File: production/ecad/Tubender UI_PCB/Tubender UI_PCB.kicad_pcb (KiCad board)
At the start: 2 copper layers, 7 parts, among them J1 640387-5, J2 1-640387-0

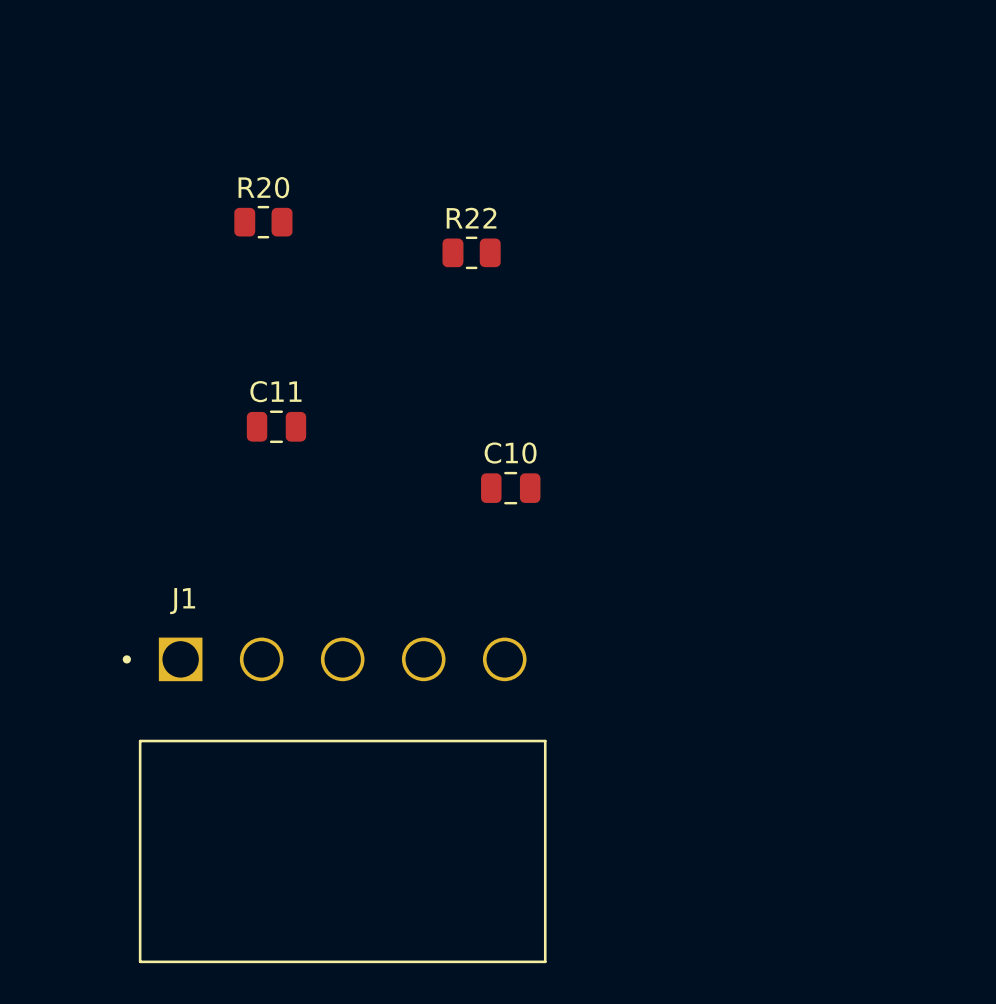
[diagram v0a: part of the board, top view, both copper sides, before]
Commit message: Some intial work for rotary encoder on  PCB
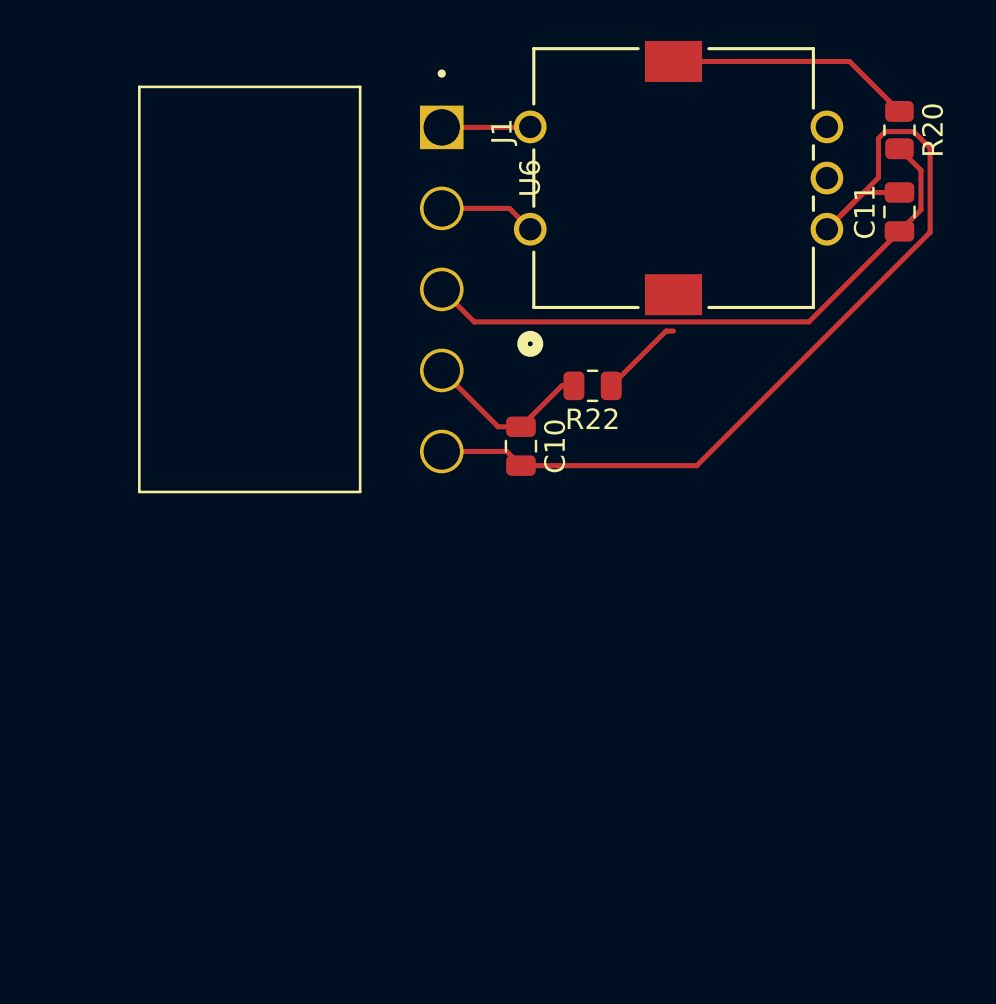
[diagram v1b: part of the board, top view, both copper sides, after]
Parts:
- added U6: PEC11R-4215K-S0024, Rotary_Encoder:SW_PEC11R-4XXXK-SXXXX_BRN, F.Cu at (217.5, 26.8)
- moved C11 32.2 mm to (235.5, 26.0), turned to 90 degrees
- moved R20 31.4 mm to (235.5, 22.0), turned to -90 degrees
- moved J1 29.0 mm to (213.1, 21.9), turned to -90 degrees
- moved R22 8.79 mm to (220.5, 34.5), turned to 180 degrees
- moved C10 2.11 mm to (217.0, 37.5), turned to -90 degrees
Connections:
- C10 pad 2: GND -> +3V3
- C11 pad 2: GND -> +3V3
- C18 pad 2: GND -> +3V3
- J1 pad 5: GND -> +3V3
- J2 pad 10: GND -> +3V3
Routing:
- net +3V3: track 0.00 -> 45.8 mm
- net DIAL_CHANNEL_B: track 0.00 -> 29.8 mm
- net Net-(U6-B): track 0.00 -> 12.1 mm
- net DIAL_CHANNEL_A: track 0.00 -> 8.43 mm
- net DIAL_BUTTON: track 0.00 -> 4.75 mm
- net +5V: track 0.00 -> 4.33 mm
- net Net-(U6-A): track 0.00 -> 4.15 mm

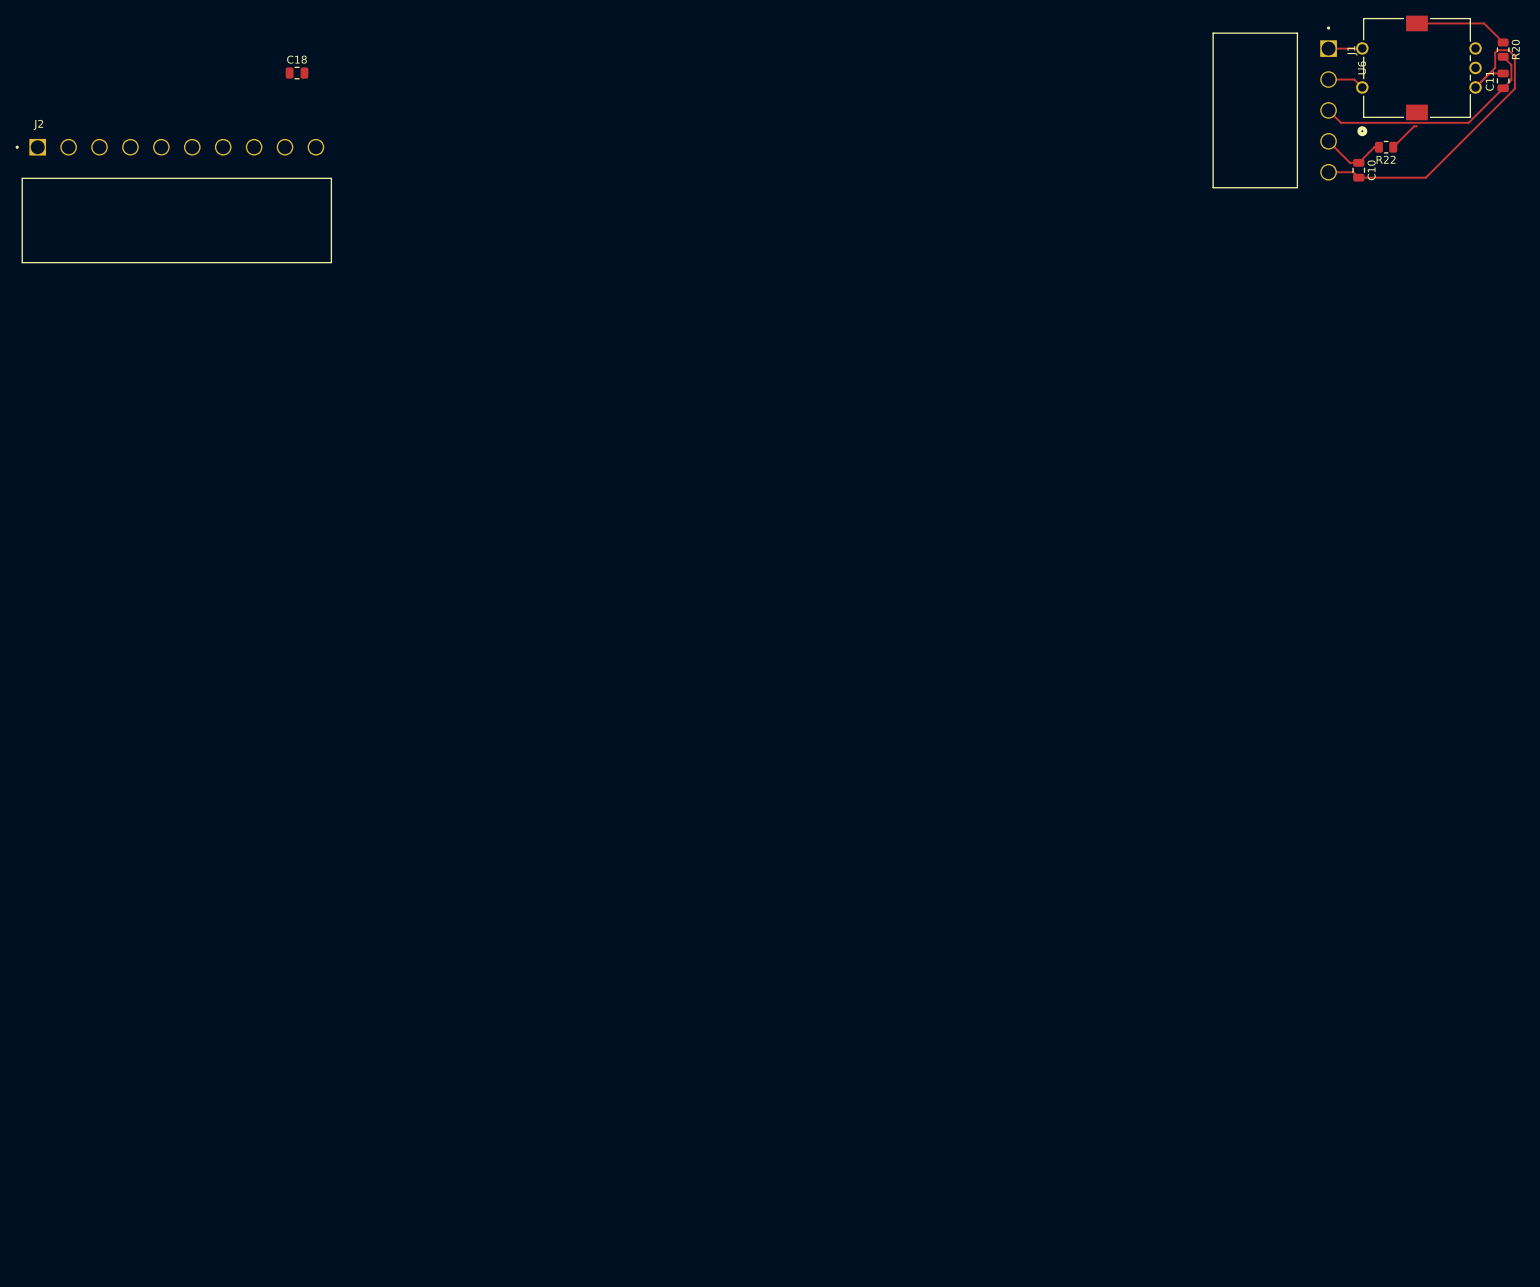
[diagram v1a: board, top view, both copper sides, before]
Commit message: Added UI footprints and first draft of layout
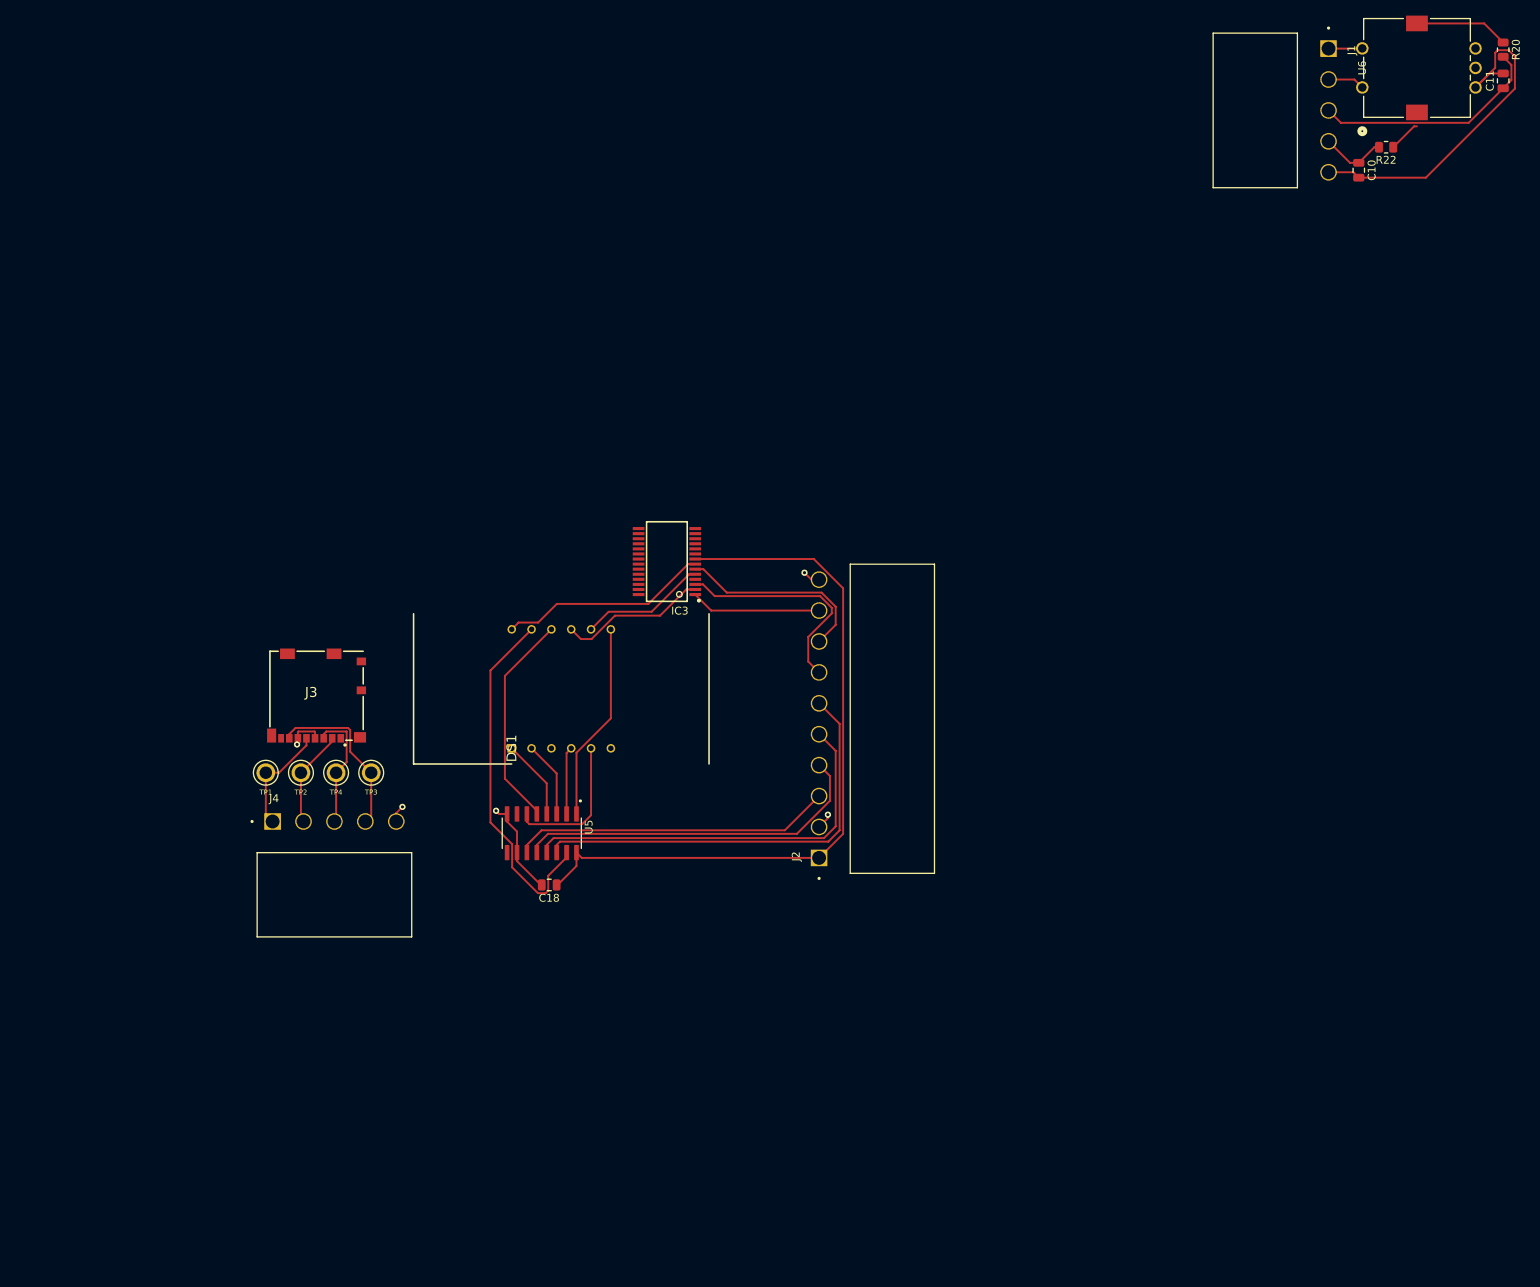
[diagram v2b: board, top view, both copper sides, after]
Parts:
- added DS1: BC56-12EWA, footprints:DIPS1524W50P254L3760H835Q12N, F.Cu at (108.5, 111.5)
- added IC3: SN74LVC1G29DCTR, footprints:SOP65P780X200-28N, F.Cu at (128.4, 87.6)
- added J3: 104031-0811, footprints:1040310811, F.Cu at (83.5, 110.5)
- added J4: 640387-5, footprints:TE_640387-5, F.Cu at (77.9, 120.9)
- added TP1: 5006, footprints:KEYSTONE_5006, F.Cu at (77.0, 114.6)
- added TP2: 5006, footprints:KEYSTONE_5006, F.Cu at (81.5, 114.6)
- added TP3: 5006, footprints:KEYSTONE_5006, F.Cu at (90.5, 114.6)
- added TP4: 5006, footprints:KEYSTONE_5006, F.Cu at (86.0, 114.6)
- added U5: 74HC595, footprints:SOIC127P600X175-16N, F.Cu at (112.3, 122.4)
- moved J2 135.3 mm to (147.9, 125.5), turned to 90 degrees
- moved C18 108.9 mm to (113.3, 129.0), turned to 180 degrees
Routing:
- net +5V: track 4.33 -> 97.3 mm
- net 7-SEG_SER: track 0.00 -> 55.4 mm
- net 7-SEG_OEb: track 0.00 -> 51.7 mm
- net 7-SEG_RCLK: track 0.00 -> 46.0 mm
- net Net-(DS1-ANODE_A): track 0.00 -> 45.8 mm
- net 7-SEG_SRCLK: track 0.00 -> 41.0 mm
- net 7-SEG_A0: track 0.00 -> 28.8 mm
- net Net-(DS1-ANODE_F): track 0.00 -> 27.8 mm
- net Net-(DS1-COMMON_CATHODE_DIG1): track 0.00 -> 27.0 mm
- net Net-(DS1-ANODE_B): track 0.00 -> 25.5 mm
- net 7-SEG_A1: track 0.00 -> 25.3 mm
- net +3V3: track 45.8 -> 69.8 mm, vias 0 -> 5
- net SD_DAT0: track 0.00 -> 21.9 mm
- net Net-(DS1-COMMON_CATHODE_DIG2): track 0.00 -> 19.0 mm
- net Net-(DS1-ANODE_G): track 0.00 -> 18.4 mm
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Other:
- copper layers 2 -> 4

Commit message: Added Display Daughter Board PCB and start UI layout
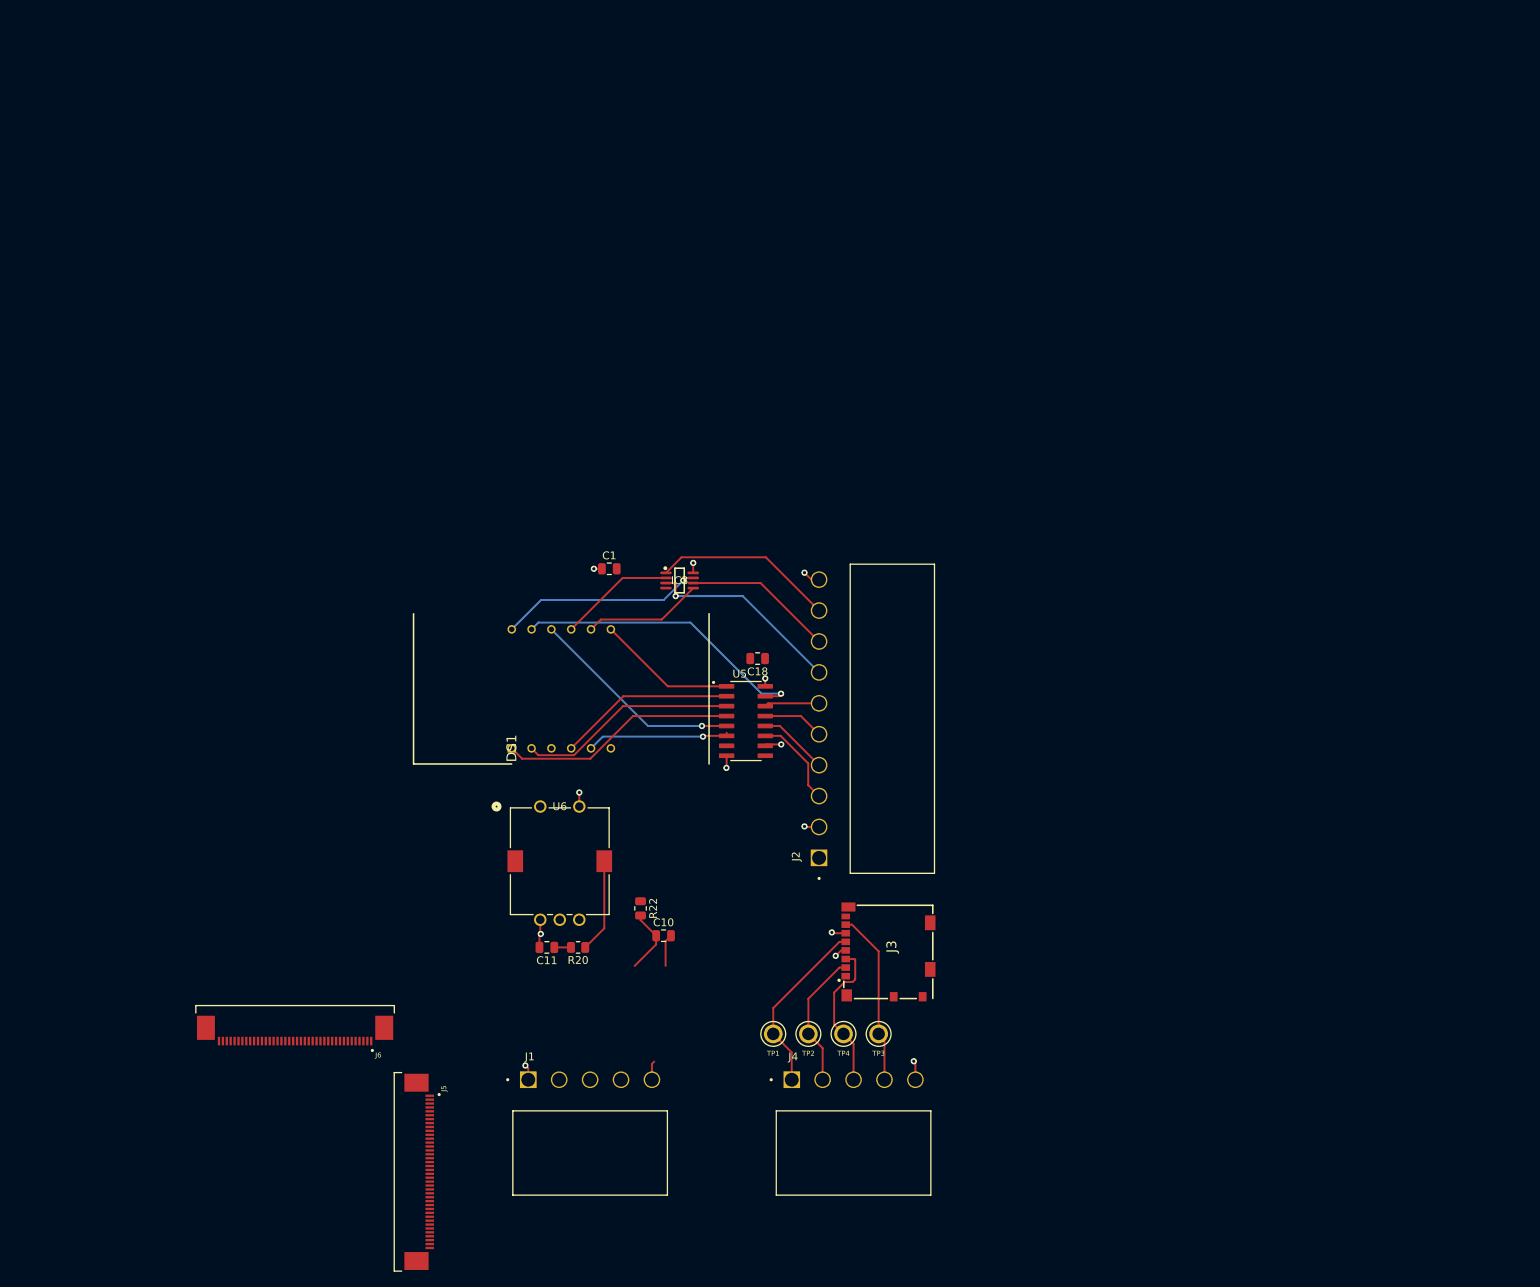
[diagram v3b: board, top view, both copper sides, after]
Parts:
- added C1: 0.1u, Capacitor_SMD:C_0805_2012Metric, F.Cu at (121.0, 88.5)
- added J5: 4-1734592-0, footprints:TE_4-1734592-0, F.Cu at (98.0, 165.8)
- added J6: 4-1734592-0, footprints:TE_4-1734592-0, F.Cu at (80.8, 149.0)
- IC3: footprint footprints:SOP65P780X200-28N -> footprints:DCT0008A_N
- moved J1 167.2 mm to (110.6, 153.9), turned to 0 degrees
- moved C11 165.3 mm to (113.0, 137.0), turned to 180 degrees
- moved R20 165.1 mm to (117.0, 137.0), turned to 180 degrees
- moved U6 139.9 mm to (112.2, 119.0), turned to 0 degrees
- moved R22 136.5 mm to (125.0, 132.0), turned to -90 degrees
- moved C10 132.5 mm to (128.0, 135.5), turned to 0 degrees
- moved J4 74.3 mm to (144.4, 153.9)
- moved TP1 73.1 mm to (142.0, 148.1)
- moved TP2 73.1 mm to (146.5, 148.1)
- moved TP3 73.1 mm to (155.5, 148.1)
- moved TP4 73.1 mm to (151.0, 148.1)
- moved J3 72.8 mm to (151.0, 137.6), turned to -90 degrees
- moved C18 39.4 mm to (140.0, 100.0)
- moved U5 29.8 mm to (138.5, 108.0), turned to 0 degrees
- moved IC3 2.92 mm to (130.0, 90.0), turned to 0 degrees
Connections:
- C10 pad 2: +3V3 -> GND
- C11 pad 2: +3V3 -> GND
- C18 pad 2: +3V3 -> GND
- IC3 pad 4: +3V3 -> GND
- J1 pad 5: +3V3 -> GND
- J2 pad 10: +3V3 -> GND
- J3 pad 6: +3V3 -> GND
- J4 pad 5: +3V3 -> GND
- U5 pad 8: +3V3 -> GND
- U6 pad 5: +3V3 -> GND
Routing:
- net +5V: track 97.3 -> 6.13 mm, vias 0 -> 4
- net +3V3: track 69.8 -> 6.06 mm, vias 5 -> 4
- net 7-SEG_SER: track 55.4 -> 7.05 mm
- net 7-SEG_OEb: track 51.7 -> 7.86 mm
- net 7-SEG_RCLK: track 46.0 -> 8.97 mm
- net 7-SEG_SRCLK: track 41.0 -> 11.7 mm
- net DIAL_CHANNEL_B: track 29.8 -> 2.14 mm
- net Net-(DS1-ANODE_E): track 10.3 -> 30.3 mm
- net GND: track 0.00 -> 18.4 mm, vias 0 -> 5
- net Net-(DS1-ANODE_D): track 9.74 -> 27.9 mm
- net Net-(DS1-ANODE_C): track 8.65 -> 22.7 mm
- net SD_CLK: track 14.2 -> 23.0 mm
- net Net-(DS1-ANODE_B): track 25.5 -> 17.8 mm
- net Net-(DS1-ANODE_A): track 45.8 -> 38.3 mm, vias 0 -> 1
- net 7-SEG_Gb: track 16.7 -> 23.3 mm
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- added copper zone on In2.Cu, net GND

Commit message: Finished First Draft Layout of UI PCB
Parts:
- removed J5, J6: 4-1734592-0, footprints:TE_4-1734592-0
- IC3: footprint footprints:DCT0008A_N -> footprints:SOP65P400X130-8N
- moved C1 39.4 mm to (144.0, 120.5), turned to 90 degrees
- moved C10 23.6 mm to (104.5, 132.5), turned to -90 degrees
- moved R22 20.9 mm to (104.5, 127.9)
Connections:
- J2 pad 1: +5V -> GND
- J2 pad 10: GND -> +5V
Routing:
- net DIAL_BUTTON: track 0.00 -> 36.0 mm
- net DIAL_CHANNEL_A: track 8.43 -> 32.6 mm
- net DIAL_CHANNEL_B: track 2.14 -> 20.2 mm, vias 0 -> 1
- net GND: track 18.4 -> 13.1 mm, vias 5 -> 6
- net Net-(U6-A): track 0.00 -> 4.89 mm
- net +5V: track 6.13 -> 9.67 mm
- net +3V3: track 6.06 -> 7.03 mm, vias 4 -> 2
- added copper zone on In1.Cu, net +3V3
- added copper zone on In1.Cu, net +5V
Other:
- board outline added: 72.5 x 87.5 mm
